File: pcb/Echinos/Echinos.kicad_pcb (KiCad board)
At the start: 2 copper layers, 167.4 x 137.7 mm, 90 parts, among them J1 Conn_01x06_Socket, J2 Conn_01x06_Socket, J3 Conn_01x06_Socket, J5 SATA-7p, J6 USB_B_Micro, J7 Conn_01x04_Socket, SW1 Reset, SW111 SW_Push, SW112 SW_Push, SW113 SW_Push, SW114 SW_Push, SW115 SW_Push, SW122 SW_Push, SW123 SW_Push, SW124 SW_Push, SW125 SW_Push, SW131 SW_Push, SW132 SW_Push, SW133 SW_Push, SW134 SW_Push, SW135 SW_Push, SW141 SW_Push, SW142 SW_Push, SW143 SW_Push, SW144 SW_Push, SW145 SW_Push, SW151 SW_Push, SW152 SW_Push, SW153 SW_Push, SW154 SW_Push, SW155 SW_Push, U1 Helios, U7 SRV05-4

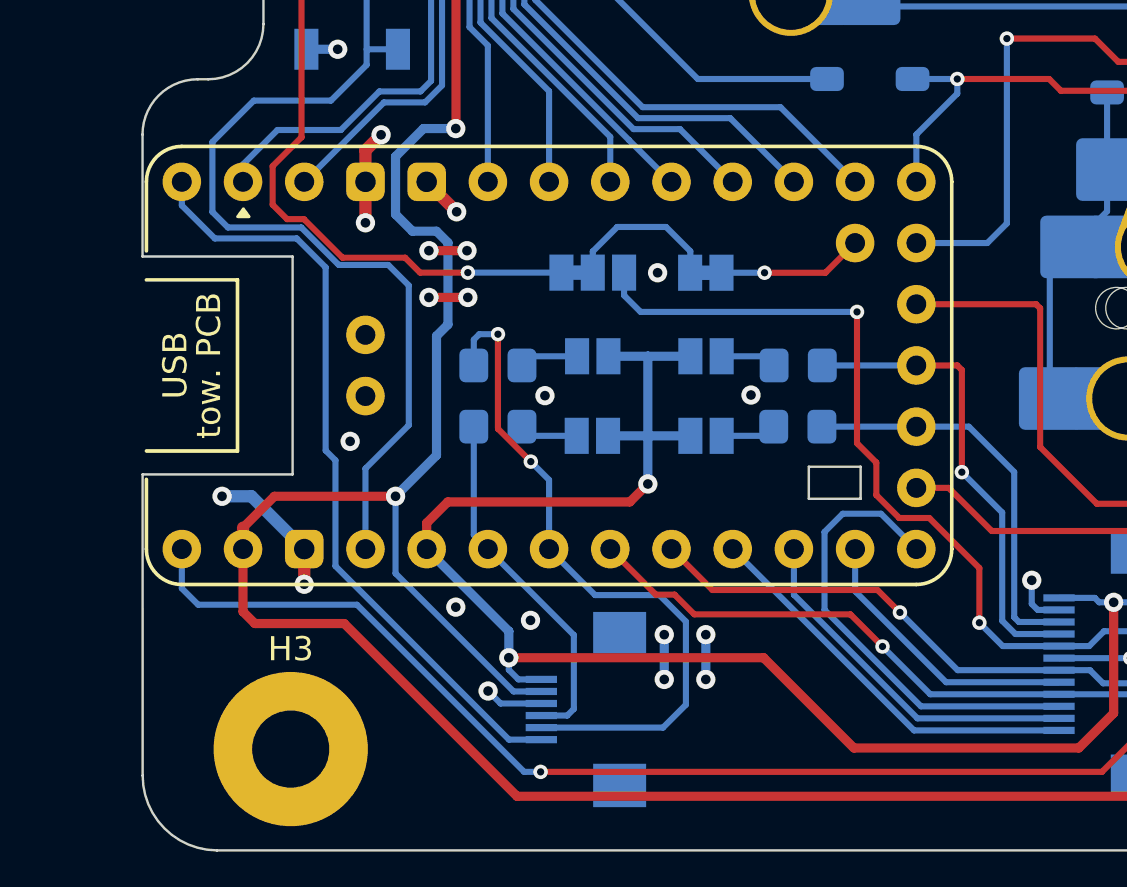
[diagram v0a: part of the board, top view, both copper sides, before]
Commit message: [PCB] - Save last state with Helios MCU board.   - Move helios PCB on the bottom side to avoid conflict while typing on the outer pinky key   - Improve helios PCB (both top and bottom) with PCB edge, orientation information, standardization of holes sizes
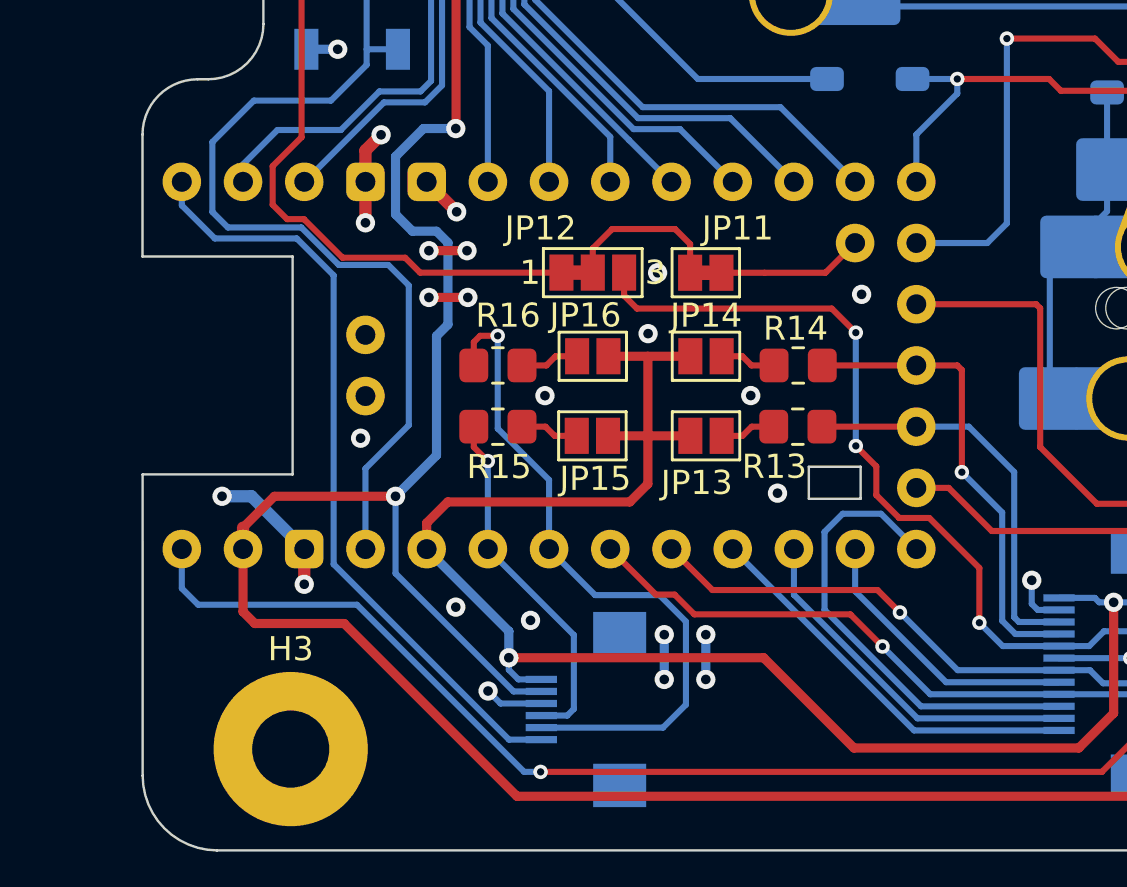
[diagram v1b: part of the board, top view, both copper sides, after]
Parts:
- JP11, JP12, JP13, JP14, JP15, JP16, R13, R14, R15, R16: moved to F.Cu
- U1: footprint Echinos:Helios_AH_USBdn -> Echinos:Helios_AH_USBup; moved to B.Cu
- turned U1 to -90 degrees
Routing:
- net rgb_out: track 88.4 -> 88.0 mm, vias 4 -> 5
- net ps2_clk: track 28.7 -> 28.6 mm, vias 2 -> 1
- net +3.3V: vias 3 -> 2
- net ps2_data: vias 0 -> 1
- net /Backlight/backlight_in: vias 2 -> 1
- net rgb: vias 1 -> 0
- net GND: vias 57 -> 60

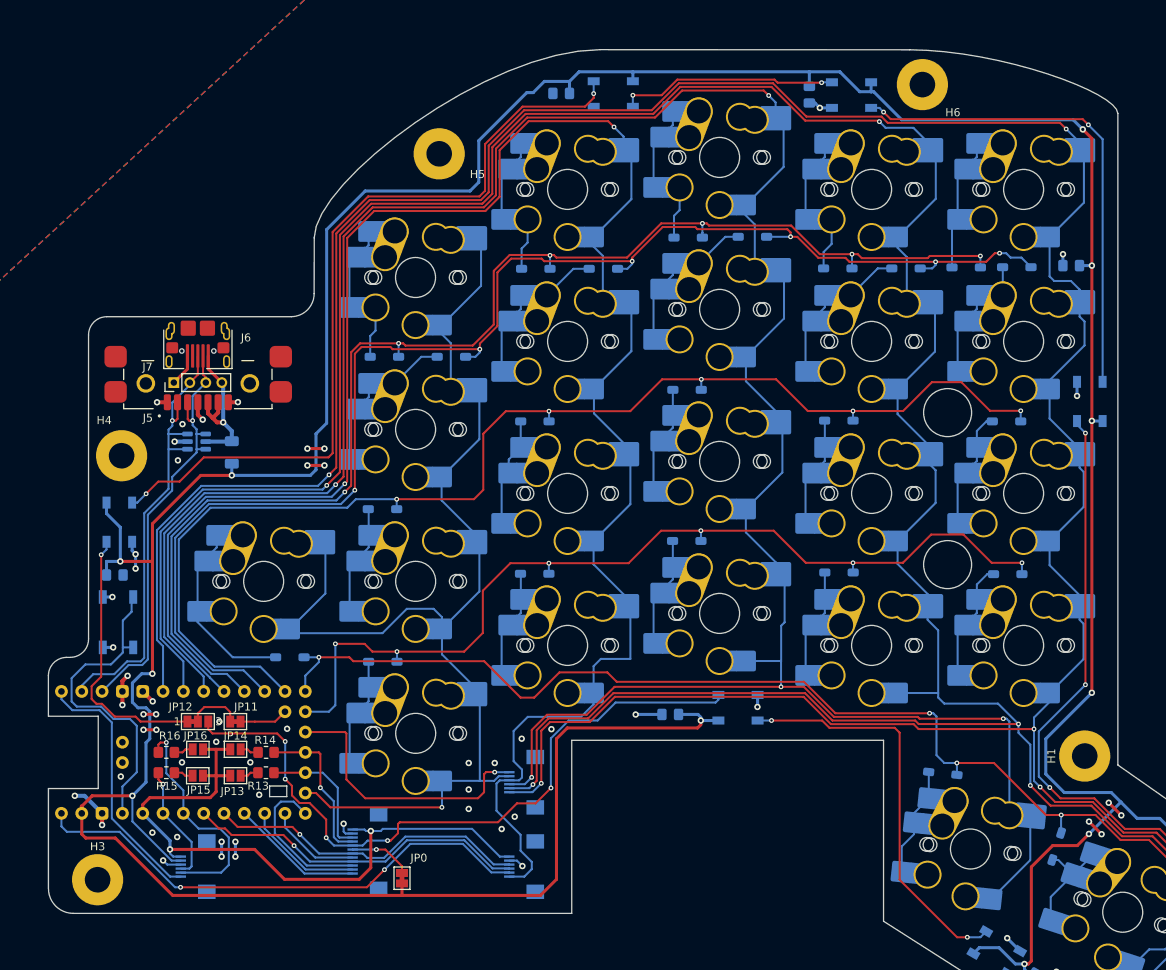
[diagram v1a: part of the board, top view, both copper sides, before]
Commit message: [PCB] - Save last state with Helios MCU board and on board USB-C.
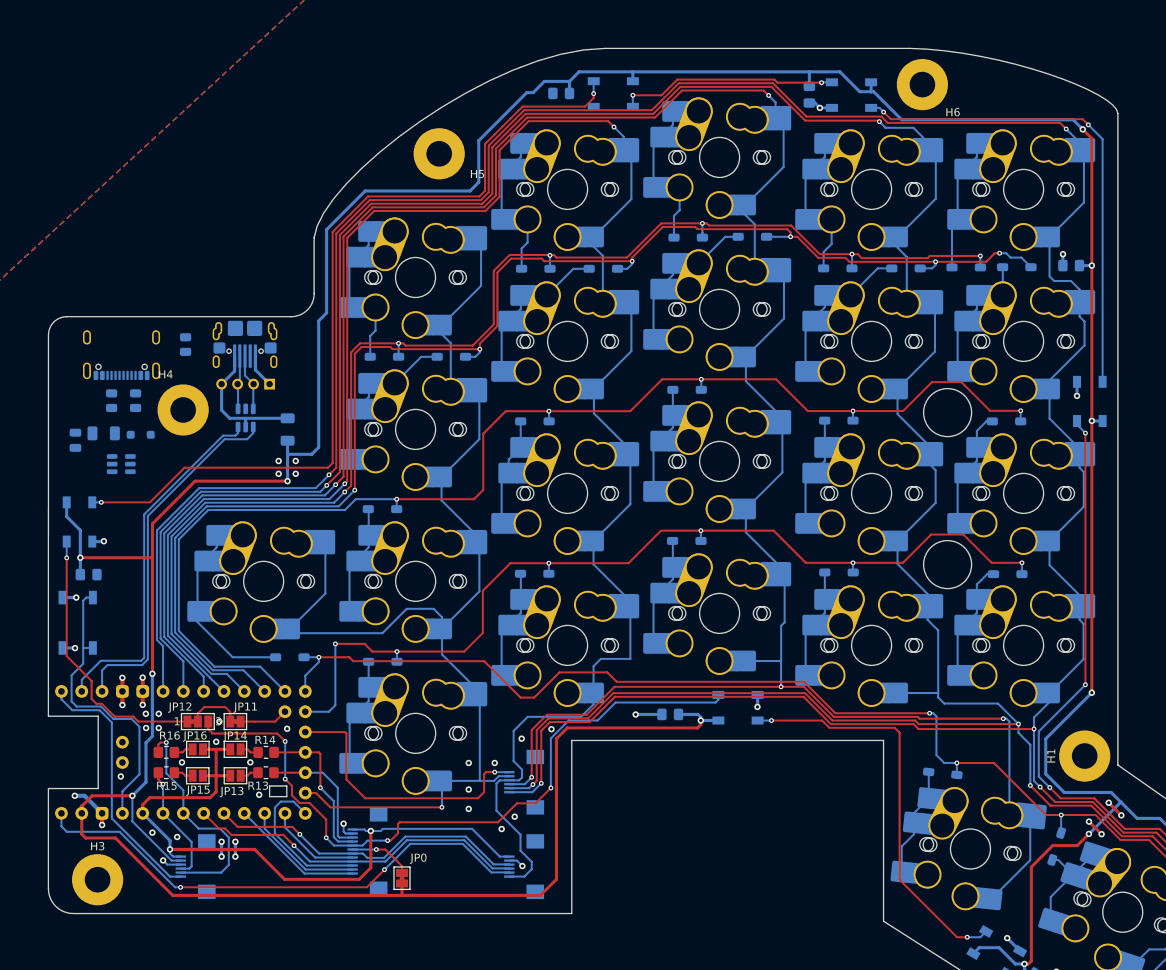
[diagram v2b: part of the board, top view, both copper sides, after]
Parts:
- removed J5: SATA-7p, Echinos:SATA_1x07_P1.27mm_pads_SMD
- added C3: 10u, Capacitor_SMD:C_0805_2012Metric, B.Cu at (49.5, 95.8)
- added D3: B5817WS, Diode_SMD:D_SOD-323_HandSoldering, B.Cu at (57.6, 95.1)
- added F3: 500mA, Fuse:Fuse_1206_3216Metric, B.Cu at (53.0, 94.9)
- added FB1: 600R, Resistor_SMD:R_0805_2012Metric, B.Cu at (63.2, 83.8)
- added J8: USB_C_Receptacle_USB2.0, Connector_USB:USB_C_Receptacle_GCT_USB4105-xx-A_16P_TopMnt_Horizontal, B.Cu at (55.2, 84.0)
- added R7: 5.1k, Resistor_SMD:R_0805_2012Metric, B.Cu at (57.0, 90.8)
- added R8: 5.1k, Resistor_SMD:R_0805_2012Metric, B.Cu at (54.0, 90.8)
- added U2: USBLC6-2P6, Package_TO_SOT_SMD:SOT-23-6, B.Cu at (55.2, 98.7)
- J6, J7: moved to B.Cu
- U7: value SRV05-4 -> USBLC6-2P6
- moved J7 12.0 mm to (73.8, 88.7)
- moved H4 9.59 mm to (62.9, 92.0)
- moved F2 7.54 mm to (76.0, 94.4)
- moved U7 6.81 mm to (70.8, 93.0), turned to -90 degrees
- moved J6 5.90 mm to (70.7, 83.0), turned to 0 degrees
- moved SW1 5.04 mm to (49.8, 118.6)
- moved D11 4.98 mm to (50.0, 106.0)
- moved C11 3.27 mm to (51.1, 112.5)
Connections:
- J6 pad 2: RX -> P_TX
- J6 pad 3: TX -> P_RX
- J7 pad 2: TX -> P_RX
- J7 pad 3: RX -> P_TX
- U7 pad 1: TX -> P_TX
- U7 pad 3: TX -> P_RX
- U7 pad 6: RX -> TX
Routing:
- net GND: track 69.3 -> 55.0 mm, vias 60 -> 54
- net TX: track 58.3 -> 45.3 mm, vias 1 -> 0
- net RX: track 54.0 -> 45.1 mm, vias 1 -> 0
- net P_RX: track 0.00 -> 7.05 mm
- net P_TX: track 0.00 -> 6.77 mm
- net Net-(D11-DOUT): track 100.3 -> 106.0 mm
- net VBUS_split: track 21.2 -> 17.2 mm, vias 1 -> 0
- net reset: track 40.2 -> 37.3 mm
- net +5V: track 512.7 -> 513.5 mm
- net /Backlight/backlight_in: track 33.6 -> 34.1 mm
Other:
- board size 167.4 x 137.7 mm -> 167.4 x 137.9 mm

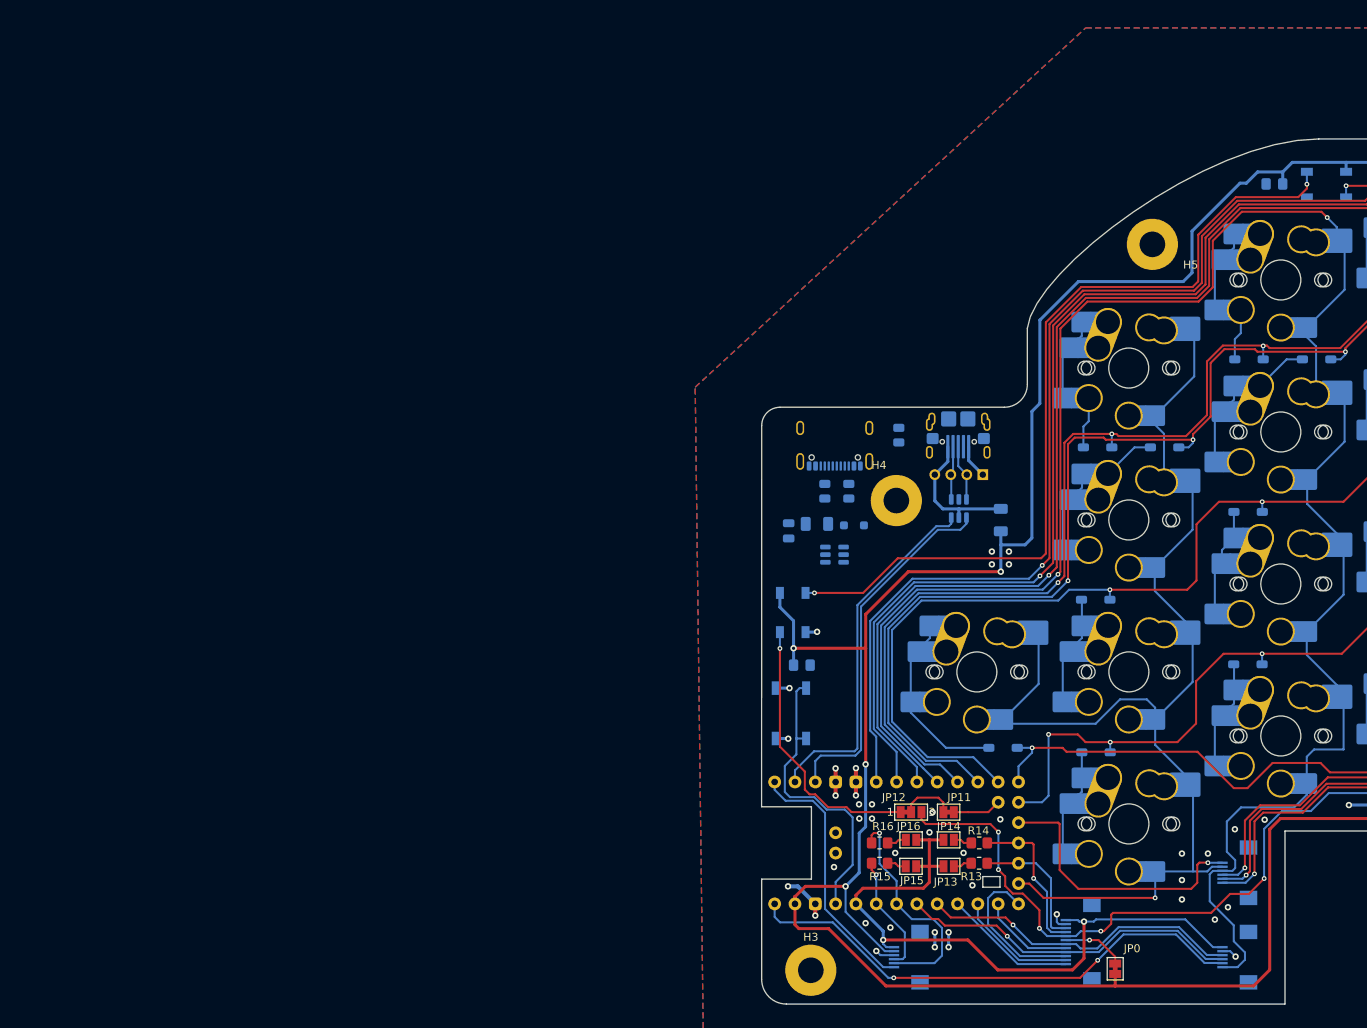
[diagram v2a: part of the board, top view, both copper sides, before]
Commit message: [PCB] - Save last state with on board RP2040.
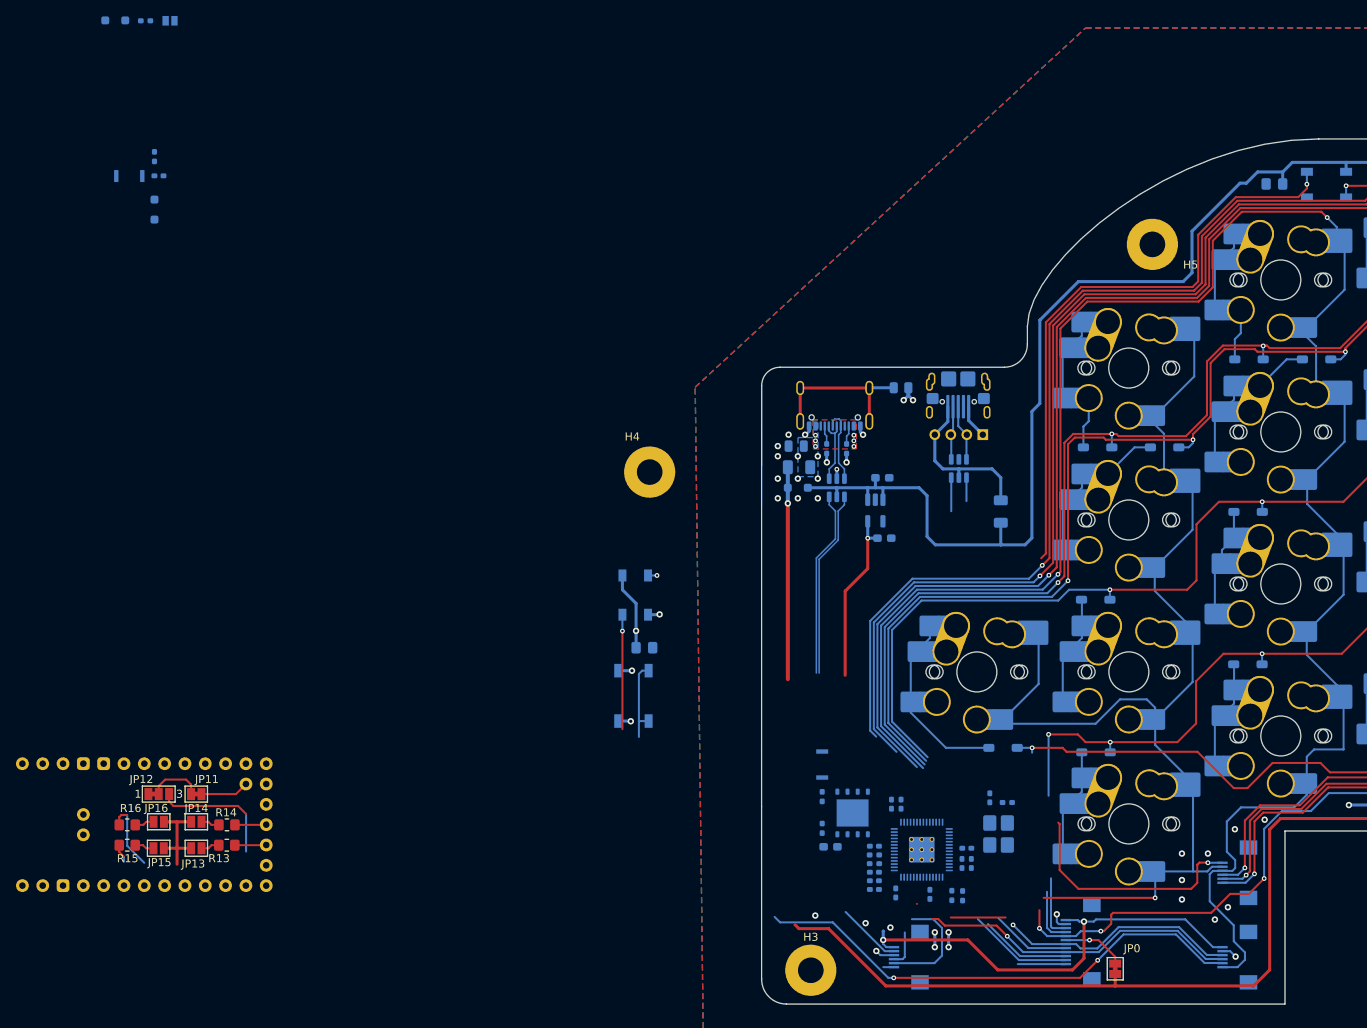
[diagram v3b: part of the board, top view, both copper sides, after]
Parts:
- added C1: 1µ, Capacitor_SMD:C_0603_1608Metric_Pad1.08x0.95mm_HandSolder, B.Cu at (61.2, 89.1)
- added C10: 100n, Capacitor_SMD:C_0402_1005Metric_Pad0.74x0.62mm_HandSolder, B.Cu at (62.3, 129.9)
- added C18: 100n, Capacitor_SMD:C_0402_1005Metric_Pad0.74x0.62mm_HandSolder, B.Cu at (67.1, 141.2)
- added C19: 100n, Capacitor_SMD:C_0402_1005Metric_Pad0.74x0.62mm_HandSolder, B.Cu at (71.7, 135.4)
- added C2: 4.7µ, Capacitor_SMD:C_0603_1608Metric_Pad1.08x0.95mm_HandSolder, B.Cu at (61.4, 96.7)
- added C20: 1u, Capacitor_SMD:C_0402_1005Metric_Pad0.74x0.62mm_HandSolder, B.Cu at (62.9, 141.0)
- added C21: 100n, Capacitor_SMD:C_0402_1005Metric_Pad0.74x0.62mm_HandSolder, B.Cu at (60.2, 140.6)
- added C22: 100n, Capacitor_SMD:C_0402_1005Metric_Pad0.74x0.62mm_HandSolder, B.Cu at (63.5, 129.9)
- added C23: 100n, Capacitor_SMD:C_0402_1005Metric_Pad0.74x0.62mm_HandSolder, B.Cu at (60.2, 139.5)
- added C24: 100n, Capacitor_SMD:C_0402_1005Metric_Pad0.74x0.62mm_HandSolder, B.Cu at (60.2, 135.2)
- added C4: 1µ, Capacitor_SMD:C_0603_1608Metric_Pad1.08x0.95mm_HandSolder, B.Cu at (54.7, 135.3)
- added C5: 0.1µF, Capacitor_SMD:C_0402_1005Metric_Pad0.74x0.62mm_HandSolder, B.Cu at (74.6, 129.1)
- added C6: 1u, Capacitor_SMD:C_0402_1005Metric_Pad0.74x0.62mm_HandSolder, B.Cu at (-29.2, 51.4)
- added C7: 100n, Capacitor_SMD:C_0402_1005Metric_Pad0.74x0.62mm_HandSolder, B.Cu at (71.1, 137.3)
- added C8: 100n, Capacitor_SMD:C_0402_1005Metric_Pad0.74x0.62mm_HandSolder, B.Cu at (72.3, 137.3)
- added C9: 1u, Capacitor_SMD:C_0402_1005Metric_Pad0.74x0.62mm_HandSolder, B.Cu at (60.2, 138.4)
- added D1: LED, Diode_SMD:D_SOD-323_HandSoldering, B.Cu at (-34.7, 32.0)
- added D2: 1N4148, Diode_SMD:D_SOD-323_HandSoldering, B.Cu at (-29.8, 55.6)
- added JP205: 3x3_LED_jumper, Echinos:SolderJumper_Open_0.8x1.2mm, B.Cu at (-27.8, 32.0)
- added R1: 10k, Resistor_SMD:R_0402_1005Metric_Pad0.72x0.64mm_HandSolder, B.Cu at (71.2, 141.4)
- added R10: 27, Resistor_SMD:R_0402_1005Metric_Pad0.72x0.64mm_HandSolder, B.Cu at (60.2, 136.3)
- added R11: 27, Resistor_SMD:R_0402_1005Metric_Pad0.72x0.64mm_HandSolder, B.Cu at (60.2, 137.4)
- added R12: 5.1k, Resistor_SMD:R_0402_1005Metric_Pad0.72x0.64mm_HandSolder, B.Cu at (69.9, 141.3)
- added R2: 1k, Resistor_SMD:R_0402_1005Metric_Pad0.72x0.64mm_HandSolder, B.Cu at (53.7, 129.0)
- added R4: 10k, Resistor_SMD:R_0402_1005Metric_Pad0.72x0.64mm_HandSolder, B.Cu at (53.7, 132.9)
- added R5: 10k, Resistor_SMD:R_0402_1005Metric_Pad0.72x0.64mm_HandSolder, B.Cu at (-29.8, 49.0)
- added R6: 10k, Resistor_SMD:R_0402_1005Metric_Pad0.72x0.64mm_HandSolder, B.Cu at (76.8, 129.7)
- added R9: 1k, Resistor_SMD:R_0402_1005Metric_Pad0.72x0.64mm_HandSolder, B.Cu at (-30.9, 32.0)
- added SW2: SW_Push, Button_Switch_SMD:SW_SPST_CK_KXT3, B.Cu at (53.7, 125.0)
- added SW3: SW_Push, Button_Switch_SMD:SW_SPST_CK_KXT3, B.Cu at (-32.9, 51.4)
- added U3: XC6210B332MR-G, Package_TO_SOT_SMD:SOT-23-5_HandSoldering, B.Cu at (60.3, 93.2)
- added U4: W25Q128JVS, Package_SON:WSON-8-1EP_6x5mm_P1.27mm_EP3.4x4mm, B.Cu at (57.5, 131.0)
- added U5: RP2040, Echinos:RP2040-QFN-56, B.Cu at (66.1, 135.6)
- added X1: CMOS -12MHz, Oscillator:Oscillator_SMD_Abracon_ASE-4Pin_3.2x2.5mm_HandSoldering, B.Cu at (75.7, 133.7)
- R7, R8: footprint Resistor_SMD:R_0805_2012Metric -> Resistor_SMD:R_0402_1005Metric_Pad0.72x0.64mm_HandSolder
- moved JP11 94.1 mm to (-24.6, 128.7)
- moved JP12 94.1 mm to (-29.3, 128.7)
- moved JP13 94.1 mm to (-24.6, 135.4)
- moved JP14 94.1 mm to (-24.6, 132.1)
- moved JP15 94.1 mm to (-29.3, 135.4)
- moved JP16 94.1 mm to (-29.3, 132.1)
- moved R13 94.1 mm to (-20.7, 135.1)
- moved R14 94.1 mm to (-20.7, 132.5)
- moved R15 94.1 mm to (-33.2, 135.1)
- moved R16 94.1 mm to (-33.2, 132.5)
- moved U1 94.1 mm to (-29.8, 132.5)
- moved H4 31.0 mm to (32.1, 88.4)
- moved C11 19.8 mm to (31.4, 110.4)
- moved D11 19.8 mm to (30.3, 103.8)
- moved SW1 19.8 mm to (30.1, 116.4)
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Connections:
- net Net-(C3-Pad1) renamed VBUS_RAW
- net Net-(D3-A) renamed VBUS
- D3 pad 1: VBUS_safe -> +5V
- U2 pad 1: /P_USB+ -> /P_USB-
- U2 pad 3: /P_USB- -> /P_USB+
- U2 pad 4: /USB- -> /USB+
- U2 pad 5: VBUS_safe -> +5V
- U2 pad 6: /USB+ -> /USB-
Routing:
- net +5V: track 513.5 -> 469.9 mm, vias 11 -> 8
- net RX: track 45.1 -> 2.94 mm
- net TX: track 45.3 -> 4.20 mm
- net ps2_reset: track 32.1 -> 1.34 mm
- net Net-(D11-DOUT): track 106.0 -> 75.9 mm
- net reset: track 37.3 -> 10.5 mm
- net VBUS: track 0.00 -> 26.5 mm, vias 0 -> 1
- net /USB-: track 0.00 -> 23.3 mm
- net /USB+: track 0.00 -> 23.3 mm
- net Net-(J8-SHIELD): track 0.00 -> 20.1 mm
- net /Backlight/backlight_in: track 34.1 -> 14.3 mm
- net sck1: track 16.7 -> 6.02 mm
- net row3: track 156.4 -> 146.3 mm
- net /P_USB+: track 0.00 -> 9.87 mm
- net scl1: track 19.6 -> 11.0 mm, vias 1 -> 0
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- added copper zone on B.Cu, net VBUS_RAW
- added copper zone on F.Cu, net VBUS_RAW
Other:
- outline, holes or cut-outs redrawn
